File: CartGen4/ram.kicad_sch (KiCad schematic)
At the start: 5 parts, among them U5 AS1C8M16PL-70BIN

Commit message: Converted footprints
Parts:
- U5: footprint BGA49C50P7X7_400X400X100 -> SamacSys_Parts:BGA49C50P7X7_400X400X100
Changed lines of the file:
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@@
     (property "Reference" "U5" (id 0) (at 139.7 45.72 0))
     (property "Value" "AS1C8M16PL-70BIN" (id 1) (at 139.7 48.26 0))
-    (property "Footprint" "BGA49C50P7X7_400X400X100" (id 2) (at 152.4 50.8 0)
+    (property "Footprint" "SamacSys_Parts:BGA49C50P7X7_400X400X100" (id 2) (at 152.4 50.8 0)
       (effects (font (size 1.27 1.27)) (justify left) hide)
     )

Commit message: Assigned and made a few footprints
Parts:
- C26, C27, C28, C29: footprint (none) -> Capacitor_SMD:C_0402_1005Metric_Pad0.74x0.62mm_HandSolder
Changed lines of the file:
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@@
       (effects (font (size 1.27 1.27)) (justify left))
     )
-    (property "Footprint" "" (id 2) (at 50.4952 173.99 0)
+    (property "Footprint" "Capacitor_SMD:C_0402_1005Metric_Pad0.74x0.62mm_HandSolder" (id 2) (at 50.4952 173.99 0)
       (effects (font (size 1.27 1.27)) hide)
     )
@@
       (effects (font (size 1.27 1.27)) (justify left))
     )
-    (property "Footprint" "" (id 2) (at 88.5952 173.99 0)
+    (property "Footprint" "Capacitor_SMD:C_0402_1005Metric_Pad0.74x0.62mm_HandSolder" (id 2) (at 88.5952 173.99 0)
       (effects (font (size 1.27 1.27)) hide)
     )
@@
       (effects (font (size 1.27 1.27)) (justify left))
     )
-    (property "Footprint" "" (id 2) (at 63.1952 173.99 0)
+    (property "Footprint" "Capacitor_SMD:C_0402_1005Metric_Pad0.74x0.62mm_HandSolder" (id 2) (at 63.1952 173.99 0)
       (effects (font (size 1.27 1.27)) hide)
     )
@@
       (effects (font (size 1.27 1.27)) (justify left))
     )
-    (property "Footprint" "" (id 2) (at 75.8952 173.99 0)
-      (effects (font (size 1.27 1.27)) hide)
-    )
+    (property "Footprint" "Capacitor_SMD:C_0402_1005Metric_Pad0.74x0.62mm_HandSolder" (id 2) (at 75.8952 173.99 0)
+      (effects (font (size 1.27 1.27)) hide)
+    )

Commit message: Assigned all footprints
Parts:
- C26, C27, C28, C29: footprint Capacitor_SMD:C_0402_1005Metric_Pad0.74x0.62mm_HandSolder -> Capacitor_SMD:C_0603_1608Metric_Pad1.08x0.95mm_HandSolder
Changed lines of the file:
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@@
       (effects (font (size 1.27 1.27)) (justify left))
     )
-    (property "Footprint" "Capacitor_SMD:C_0402_1005Metric_Pad0.74x0.62mm_HandSolder" (id 2) (at 50.4952 173.99 0)
+    (property "Footprint" "Capacitor_SMD:C_0603_1608Metric_Pad1.08x0.95mm_HandSolder" (id 2) (at 50.4952 173.99 0)
       (effects (font (size 1.27 1.27)) hide)
     )
@@
       (effects (font (size 1.27 1.27)) (justify left))
     )
-    (property "Footprint" "Capacitor_SMD:C_0402_1005Metric_Pad0.74x0.62mm_HandSolder" (id 2) (at 88.5952 173.99 0)
+    (property "Footprint" "Capacitor_SMD:C_0603_1608Metric_Pad1.08x0.95mm_HandSolder" (id 2) (at 88.5952 173.99 0)
       (effects (font (size 1.27 1.27)) hide)
     )
@@
       (effects (font (size 1.27 1.27)) (justify left))
     )
-    (property "Footprint" "Capacitor_SMD:C_0402_1005Metric_Pad0.74x0.62mm_HandSolder" (id 2) (at 63.1952 173.99 0)
+    (property "Footprint" "Capacitor_SMD:C_0603_1608Metric_Pad1.08x0.95mm_HandSolder" (id 2) (at 63.1952 173.99 0)
       (effects (font (size 1.27 1.27)) hide)
     )
@@
       (effects (font (size 1.27 1.27)) (justify left))
     )
-    (property "Footprint" "Capacitor_SMD:C_0402_1005Metric_Pad0.74x0.62mm_HandSolder" (id 2) (at 75.8952 173.99 0)
-      (effects (font (size 1.27 1.27)) hide)
-    )
+    (property "Footprint" "Capacitor_SMD:C_0603_1608Metric_Pad1.08x0.95mm_HandSolder" (id 2) (at 75.8952 173.99 0)
+      (effects (font (size 1.27 1.27)) hide)
+    )

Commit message: Changed most R and C to 0402 size
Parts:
- C26, C27, C28, C29: footprint Capacitor_SMD:C_0603_1608Metric_Pad1.08x0.95mm_HandSolder -> Capacitor_SMD:C_0402_1005Metric_Pad0.74x0.62mm_HandSolder
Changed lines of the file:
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@@
       (effects (font (size 1.27 1.27)) (justify left))
     )
-    (property "Footprint" "Capacitor_SMD:C_0603_1608Metric_Pad1.08x0.95mm_HandSolder" (id 2) (at 50.4952 173.99 0)
+    (property "Footprint" "Capacitor_SMD:C_0402_1005Metric_Pad0.74x0.62mm_HandSolder" (id 2) (at 50.4952 173.99 0)
       (effects (font (size 1.27 1.27)) hide)
     )
@@
       (effects (font (size 1.27 1.27)) (justify left))
     )
-    (property "Footprint" "Capacitor_SMD:C_0603_1608Metric_Pad1.08x0.95mm_HandSolder" (id 2) (at 88.5952 173.99 0)
+    (property "Footprint" "Capacitor_SMD:C_0402_1005Metric_Pad0.74x0.62mm_HandSolder" (id 2) (at 88.5952 173.99 0)
       (effects (font (size 1.27 1.27)) hide)
     )
@@
       (effects (font (size 1.27 1.27)) (justify left))
     )
-    (property "Footprint" "Capacitor_SMD:C_0603_1608Metric_Pad1.08x0.95mm_HandSolder" (id 2) (at 63.1952 173.99 0)
+    (property "Footprint" "Capacitor_SMD:C_0402_1005Metric_Pad0.74x0.62mm_HandSolder" (id 2) (at 63.1952 173.99 0)
       (effects (font (size 1.27 1.27)) hide)
     )
@@
       (effects (font (size 1.27 1.27)) (justify left))
     )
-    (property "Footprint" "Capacitor_SMD:C_0603_1608Metric_Pad1.08x0.95mm_HandSolder" (id 2) (at 75.8952 173.99 0)
-      (effects (font (size 1.27 1.27)) hide)
-    )
+    (property "Footprint" "Capacitor_SMD:C_0402_1005Metric_Pad0.74x0.62mm_HandSolder" (id 2) (at 75.8952 173.99 0)
+      (effects (font (size 1.27 1.27)) hide)
+    )

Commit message: Updated field information
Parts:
- C26, C27, C28, C29: Package ID (none) -> 0402
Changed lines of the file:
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@@
+      (effects (font (size 1.27 1.27)) hide)
+    )
+    (property "Description" "~" (id 7) (at 49.53 170.18 0)
+      (effects (font (size 1.27 1.27)) hide)
+    )
+    (property "MFN" "~" (id 8) (at 49.53 170.18 0)
+      (effects (font (size 1.27 1.27)) hide)
+    )
+    (property "MFP" "~" (id 9) (at 49.53 170.18 0)
+      (effects (font (size 1.27 1.27)) hide)
+    )
+    (property "Package ID" "0402" (id 10) (at 49.53 170.18 0)
       (effects (font (size 1.27 1.27)) hide)
     )
@@
       (effects (font (size 1.27 1.27)) hide)
     )
+    (property "Description" "~" (id 7) (at 87.63 170.18 0)
+      (effects (font (size 1.27 1.27)) hide)
+    )
+    (property "MFN" "~" (id 8) (at 87.63 170.18 0)
+      (effects (font (size 1.27 1.27)) hide)
+    )
+    (property "MFP" "~" (id 9) (at 87.63 170.18 0)
+      (effects (font (size 1.27 1.27)) hide)
+    )
+    (property "Package ID" "0402" (id 10) (at 87.63 170.18 0)
+      (effects (font (size 1.27 1.27)) hide)
+    )
     (pin "1")
     (pin "2")
@@
       (effects (font (size 1.27 1.27)) hide)
     )
+    (property "Description" "~" (id 7) (at 62.23 170.18 0)
+      (effects (font (size 1.27 1.27)) hide)
+    )
+    (property "MFN" "~" (id 8) (at 62.23 170.18 0)
+      (effects (font (size 1.27 1.27)) hide)
+    )
+    (property "MFP" "~" (id 9) (at 62.23 170.18 0)
+      (effects (font (size 1.27 1.27)) hide)
+    )
+    (property "Package ID" "0402" (id 10) (at 62.23 170.18 0)
+      (effects (font (size 1.27 1.27)) hide)
+    )
     (pin "1")
     (pin "2")
@@
       (effects (font (size 1.27 1.27)) hide)
     )
+    (property "Description" "~" (id 7) (at 74.93 170.18 0)
+      (effects (font (size 1.27 1.27)) hide)
+    )
+    (property "MFN" "~" (id 8) (at 74.93 170.18 0)
+      (effects (font (size 1.27 1.27)) hide)
+    )
+    (property "MFP" "~" (id 9) (at 74.93 170.18 0)
+      (effects (font (size 1.27 1.27)) hide)
+    )
+    (property "Package ID" "0402" (id 10) (at 74.93 170.18 0)
+      (effects (font (size 1.27 1.27)) hide)
+    )

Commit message: Updated some component fields
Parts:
- C26, C27, C28, C29: Supplier suggestion (none) -> https://nl.mouser.com/ProductDetail/Murata-Electronics/GRM1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; Tolerance (none) -> 20%; Voltage (none) -> 3V3
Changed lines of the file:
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@@
+      (effects (font (size 1.27 1.27)) hide)
+    )
+    (property "Supplier suggestion" "https://nl.mouser.com/ProductDetail/Murata-Electronics/GRM155R61C104KA88J?qs=sGAEpiMZZMsh%252B1woXyUXj8YF%2FGivH5Kx4uStnYyl8jU%3D" (id 11) (at 49.53 170.18 0)
+      (effects (font (size 1.27 1.27)) hide)
+    )
+    (property "Tolerance" "20%" (id 12) (at 49.53 170.18 0)
+      (effects (font (size 1.27 1.27)) hide)
+    )
+    (property "Voltage" "3V3" (id 13) (at 49.53 170.18 0)
       (effects (font (size 1.27 1.27)) hide)
     )
@@
       (effects (font (size 1.27 1.27)) hide)
     )
+    (property "Supplier suggestion" "https://nl.mouser.com/ProductDetail/Murata-Electronics/GRM155R61C104KA88J?qs=sGAEpiMZZMsh%252B1woXyUXj8YF%2FGivH5Kx4uStnYyl8jU%3D" (id 11) (at 87.63 170.18 0)
+      (effects (font (size 1.27 1.27)) hide)
+    )
+    (property "Tolerance" "20%" (id 12) (at 87.63 170.18 0)
+      (effects (font (size 1.27 1.27)) hide)
+    )
+    (property "Voltage" "3V3" (id 13) (at 87.63 170.18 0)
+      (effects (font (size 1.27 1.27)) hide)
+    )
     (pin "1")
     (pin "2")
@@
       (effects (font (size 1.27 1.27)) hide)
     )
+    (property "Supplier suggestion" "https://nl.mouser.com/ProductDetail/Murata-Electronics/GRM155R61C104KA88J?qs=sGAEpiMZZMsh%252B1woXyUXj8YF%2FGivH5Kx4uStnYyl8jU%3D" (id 11) (at 62.23 170.18 0)
+      (effects (font (size 1.27 1.27)) hide)
+    )
+    (property "Tolerance" "20%" (id 12) (at 62.23 170.18 0)
+      (effects (font (size 1.27 1.27)) hide)
+    )
+    (property "Voltage" "3V3" (id 13) (at 62.23 170.18 0)
+      (effects (font (size 1.27 1.27)) hide)
+    )
     (pin "1")
     (pin "2")
@@
       (effects (font (size 1.27 1.27)) hide)
     )
+    (property "Supplier suggestion" "https://nl.mouser.com/ProductDetail/Murata-Electronics/GRM155R61C104KA88J?qs=sGAEpiMZZMsh%252B1woXyUXj8YF%2FGivH5Kx4uStnYyl8jU%3D" (id 11) (at 74.93 170.18 0)
+      (effects (font (size 1.27 1.27)) hide)
+    )
+    (property "Tolerance" "20%" (id 12) (at 74.93 170.18 0)
+      (effects (font (size 1.27 1.27)) hide)
+    )
+    (property "Voltage" "3V3" (id 13) (at 74.93 170.18 0)
+      (effects (font (size 1.27 1.27)) hide)
+    )

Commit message: Added missing recommendations
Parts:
- U5: Supplier suggestion (none) -> https://nl.mouser.com/ProductDetail/Alliance-Memory/AS1C8M1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
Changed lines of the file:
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@@
+      (effects (font (size 1.27 1.27)) hide)
+    )
+    (property "Supplier suggestion" "https://nl.mouser.com/ProductDetail/Alliance-Memory/AS1C8M16PL-70BIN?qs=byeeYqUIh0NST7XYuCr8lQ%3D%3D" (id 11) (at 123.19 53.34 0)
       (effects (font (size 1.27 1.27)) hide)
     )

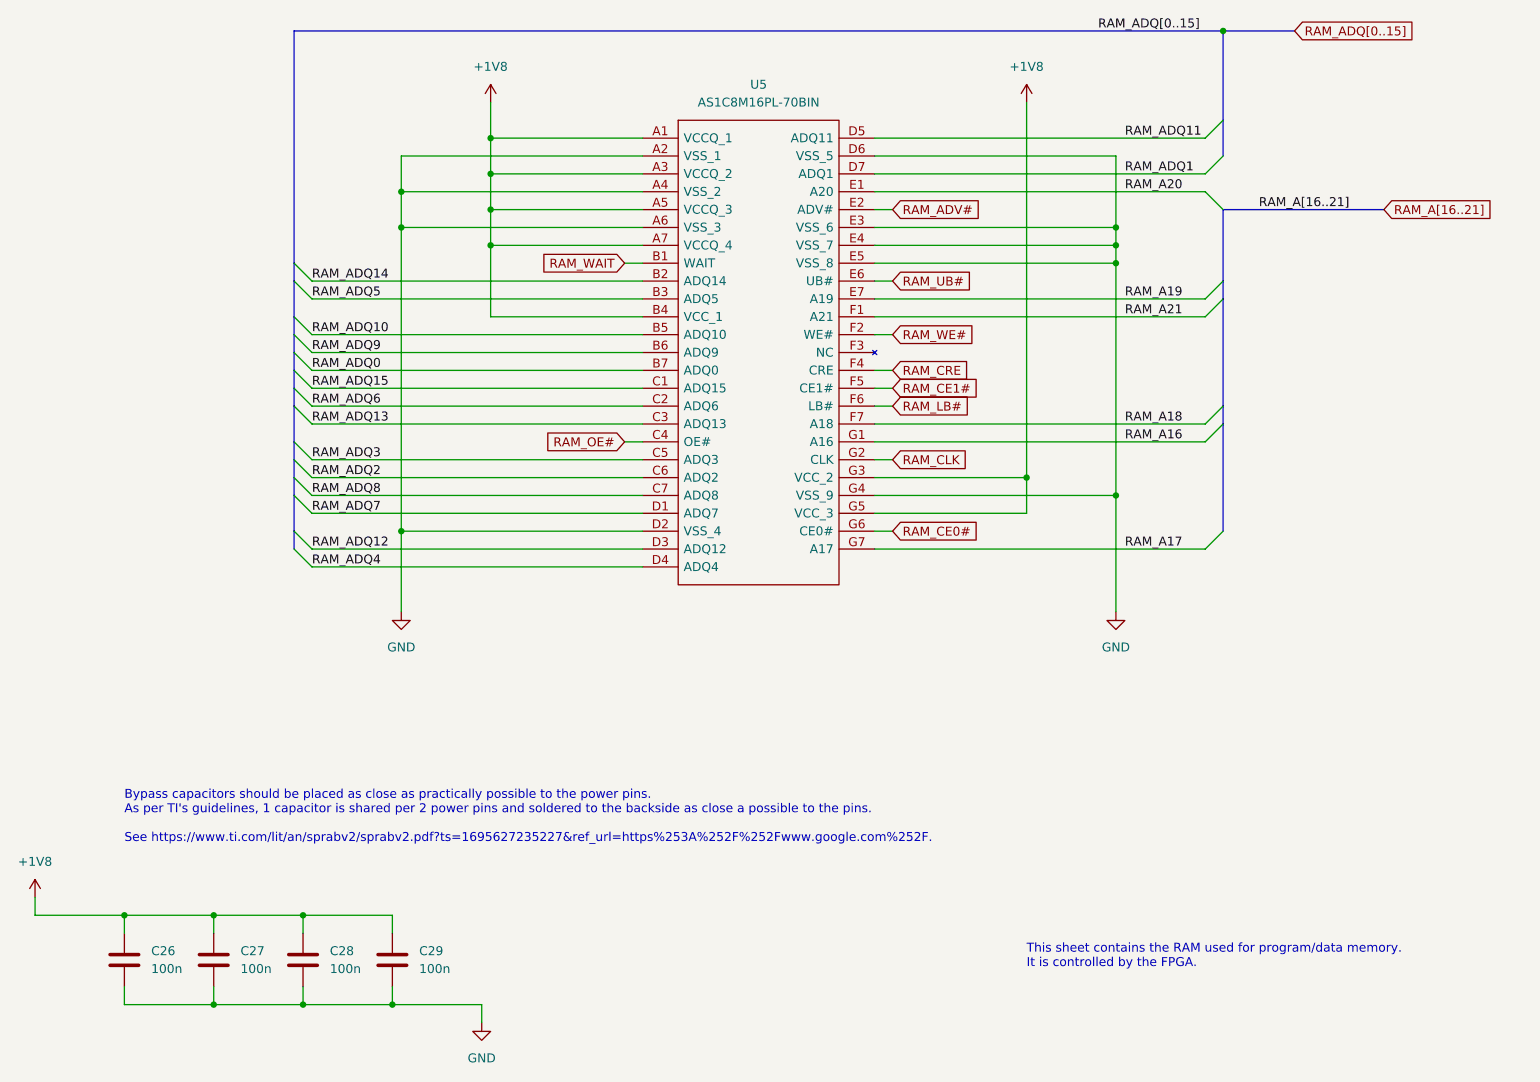
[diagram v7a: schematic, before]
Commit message: Reassigned RD geographically
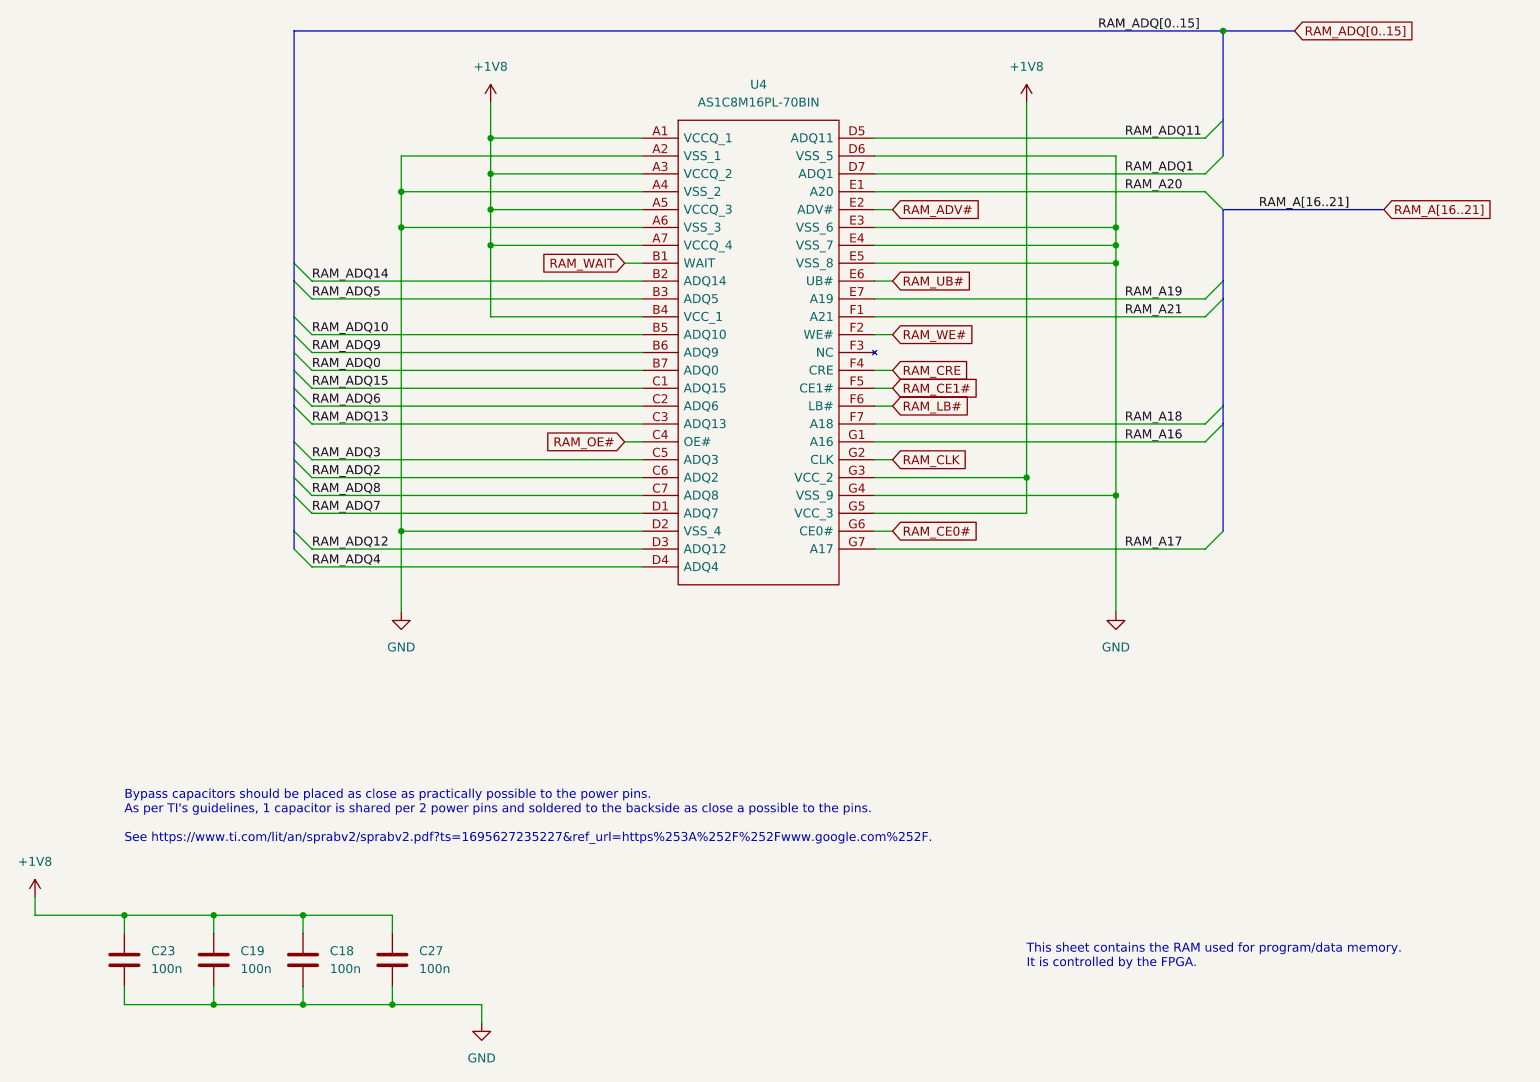
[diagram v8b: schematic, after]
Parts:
- renumbered C28 to C18, C27 to C19, C26 to C23, C29 to C27, U5 to U4
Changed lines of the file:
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@@
   (symbol (lib_id "Device:C") (at 49.53 170.18 0) (unit 1)
     (in_bom yes) (on_board yes) (fields_autoplaced)
-    (property "Reference" "C26" (id 0) (at 53.34 168.9099 0)
+    (property "Reference" "C23" (id 0) (at 53.34 168.9099 0)
       (effects (font (size 1.27 1.27)) (justify left))
     )
@@
   (symbol (lib_id "SamacSys_Parts:AS1C8M16PL-70BIN") (at 123.19 53.34 0) (unit 1)
     (in_bom yes) (on_board yes) (fields_autoplaced)
-    (property "Reference" "U5" (id 0) (at 139.7 45.72 0))
+    (property "Reference" "U4" (id 0) (at 139.7 45.72 0))
     (property "Value" "AS1C8M16PL-70BIN" (id 1) (at 139.7 48.26 0))
     (property "Footprint" "SamacSys_Parts:BGA49C50P7X7_400X400X100" (id 2) (at 152.4 50.8 0)
@@
   (symbol (lib_id "Device:C") (at 87.63 170.18 0) (unit 1)
     (in_bom yes) (on_board yes) (fields_autoplaced)
-    (property "Reference" "C29" (id 0) (at 91.44 168.9099 0)
+    (property "Reference" "C27" (id 0) (at 91.44 168.9099 0)
       (effects (font (size 1.27 1.27)) (justify left))
     )
@@
   (symbol (lib_id "Device:C") (at 62.23 170.18 0) (unit 1)
     (in_bom yes) (on_board yes) (fields_autoplaced)
-    (property "Reference" "C27" (id 0) (at 66.04 168.9099 0)
+    (property "Reference" "C19" (id 0) (at 66.04 168.9099 0)
       (effects (font (size 1.27 1.27)) (justify left))
     )
@@
   (symbol (lib_id "Device:C") (at 74.93 170.18 0) (unit 1)
     (in_bom yes) (on_board yes) (fields_autoplaced)
-    (property "Reference" "C28" (id 0) (at 78.74 168.9099 0)
-      (effects (font (size 1.27 1.27)) (justify left))
-    )
+    (property "Reference" "C18" (id 0) (at 78.74 168.9099 0)
+      (effects (font (size 1.27 1.27)) (justify left))
+    )
